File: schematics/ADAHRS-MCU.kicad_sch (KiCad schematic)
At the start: 1 part

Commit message: finished the symbol of MCU v1_01
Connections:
- net +1.5V: now reaches U-TMS570LS20216-EP1.1 (VCCIO)
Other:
- title: Ts570s -> TMS570LS MCU
- moved on the sheet: U-TMS570LS20216-EP1

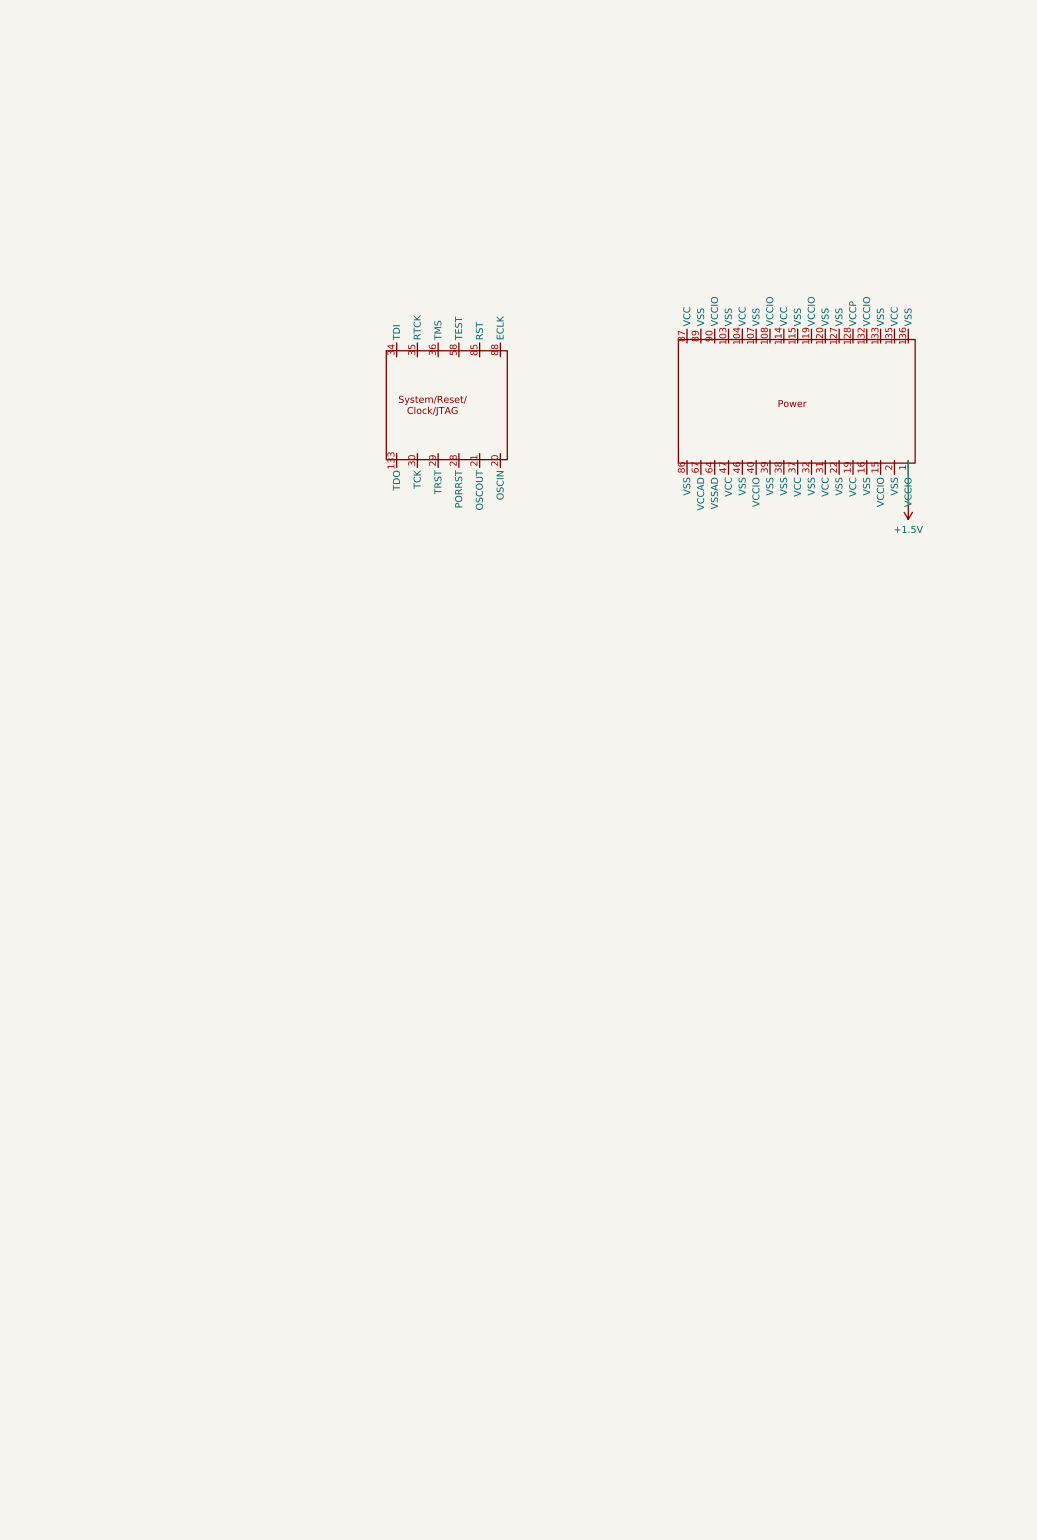
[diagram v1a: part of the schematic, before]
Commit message: finished wiring power and working on system v1.02
I had trouble with choosing and following the datasheet for the IC that supervises the supply. I had the option to doing hardware logic but it is suppose to be cheaper and having an IC suppose to be safer on the system instead of using logic.
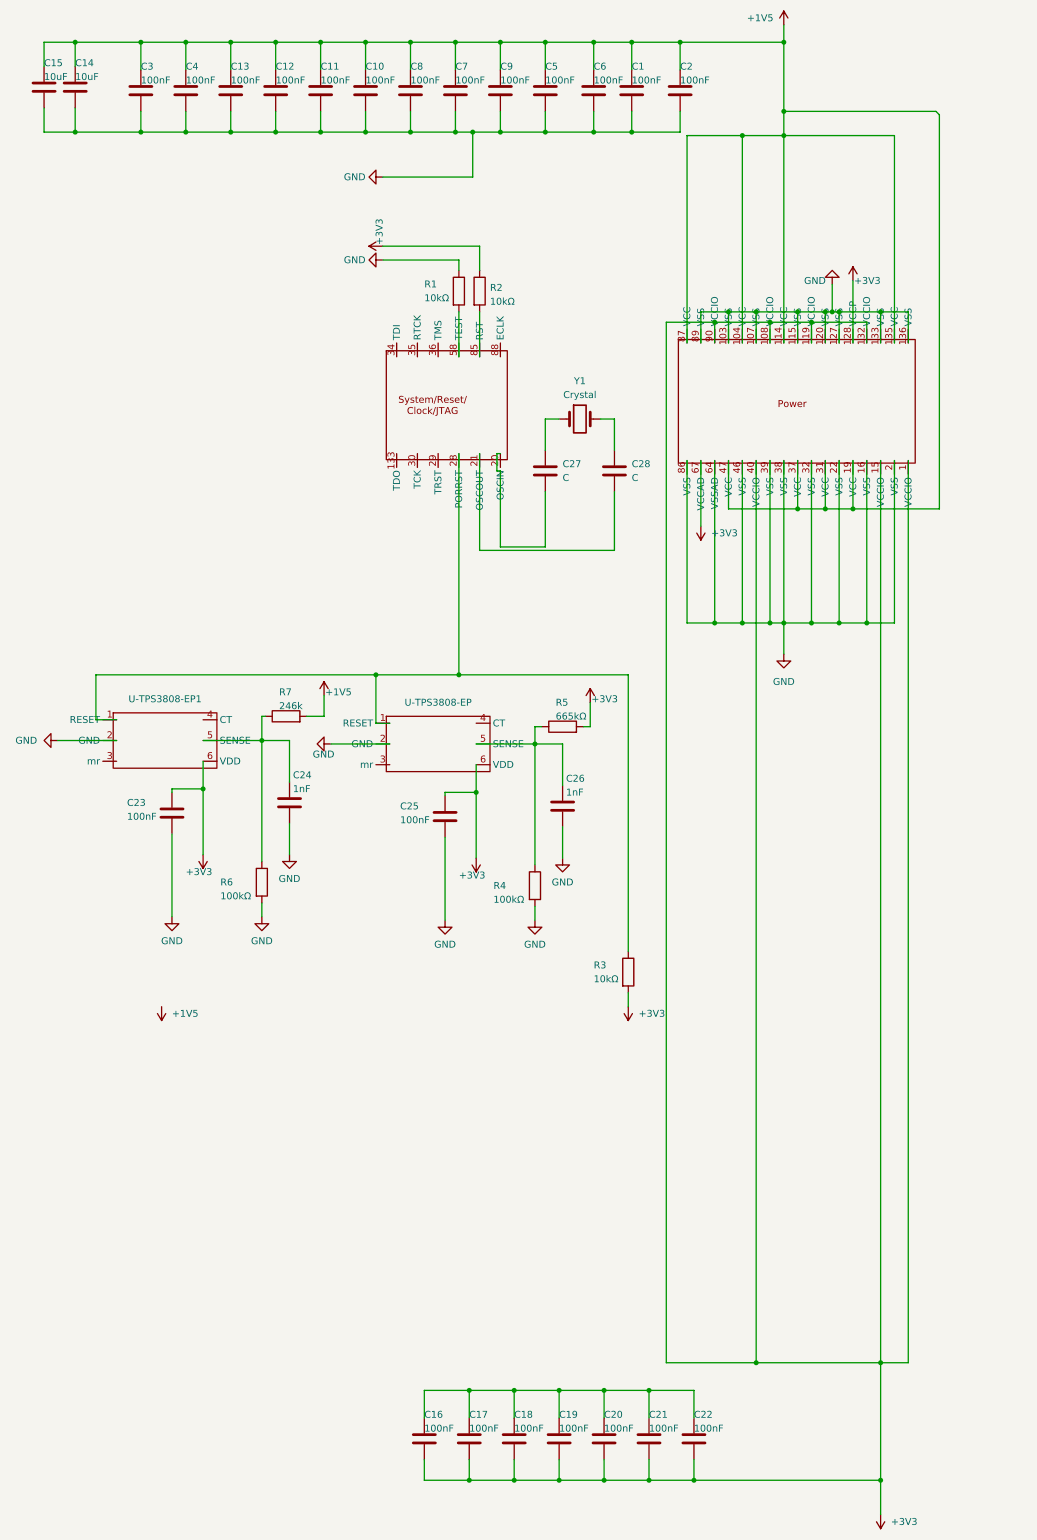
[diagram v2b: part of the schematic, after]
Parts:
- added C1, C10, C11, C12, C13, C16, C17, C18, C19, C2, C20, C21, C22, C23, C25, C3, C4, C5, C6, C7, C8, C9: 100nF, symbol Device:C
- added C14, C15: 10uF, symbol Device:C
- added C24, C26: 1nF, symbol Device:C
- added C27, C28: C, symbol Device:C
- added R1, R2, R3: 10kΩ, symbol Device:R
- added R4, R6: 100kΩ, symbol Device:R
- added R5: 665kΩ, symbol Device:R
- added R7: 246k, symbol Device:R
- added U-TPS3808-EP, U-TPS3808-EP1: ~, symbol custom:TPS3808-EP
- added Y1: Crystal, symbol Device:Crystal
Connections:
- net +1.5V is gone; now on net +3V3: U-TMS570LS20216-EP1.1 (VCCIO)
- net GND: now reaches U-TMS570LS20216-EP1.103 (VSS)
- net GND: now also U-TMS570LS20216-EP1.107 (VSS), U-TMS570LS20216-EP1.115 (VSS), U-TMS570LS20216-EP1.120 (VSS), U-TMS570LS20216-EP1.127 (VSS), U-TMS570LS20216-EP1.133 (VSS), U-TMS570LS20216-EP1.136 (VSS), U-TMS570LS20216-EP1.16 (VSS), U-TMS570LS20216-EP1.2 (VSS), U-TMS570LS20216-EP1.22 (VSS), U-TMS570LS20216-EP1.32 (VSS), U-TMS570LS20216-EP1.38 (VSS), U-TMS570LS20216-EP1.39 (VSS), U-TMS570LS20216-EP1.46 (VSS), U-TMS570LS20216-EP1.64 (VSSAD), U-TMS570LS20216-EP1.86 (VSS), U-TMS570LS20216-EP1.89 (VSS), C1.2, C10.2, C11.2, C12.2, C13.2, C14.2, C15.2, C2.2, C23.2, C24.2, C25.2, C26.2, C3.2, C4.2, C5.2, C6.2, C7.2, C8.2, C9.2, R1.1, R4.2, R6.2, U-TPS3808-EP.2 (GND), U-TPS3808-EP1.2 (GND)
- net +1V5: now reaches U-TMS570LS20216-EP1.104 (VCC)
- net +1V5: now also U-TMS570LS20216-EP1.114 (VCC), U-TMS570LS20216-EP1.135 (VCC), U-TMS570LS20216-EP1.19 (VCC), U-TMS570LS20216-EP1.31 (VCC), U-TMS570LS20216-EP1.37 (VCC), U-TMS570LS20216-EP1.47 (VCC), U-TMS570LS20216-EP1.87 (VCC), C1.1, C10.1, C11.1, C12.1, C13.1, C14.1, C15.1, C2.1, C3.1, C4.1, C5.1, C6.1, C7.1, C8.1, C9.1, R7.2
- net +3V3: now reaches U-TMS570LS20216-EP1.108 (VCCIO)
- net +3V3: now also U-TMS570LS20216-EP1.119 (VCCIO), U-TMS570LS20216-EP1.128 (VCCP), U-TMS570LS20216-EP1.132 (VCCIO), U-TMS570LS20216-EP1.15 (VCCIO), U-TMS570LS20216-EP1.40 (VCCIO), U-TMS570LS20216-EP1.67 (VCCAD), U-TMS570LS20216-EP1.90 (VCCIO), C16.2, C17.2, C18.2, C19.2, C20.2, C21.2, C22.2, C23.1, C25.1, R2.1, R3.2, R5.2, U-TPS3808-EP.6 (VDD), U-TPS3808-EP1.6 (VDD)
- net at U-TMS570LS20216-EP1.20 (OSCIN): now also C27.2
- net at U-TMS570LS20216-EP1.21 (OSCOUT): now also C28.2
- net at U-TMS570LS20216-EP1.28 (PORRST): now also R3.1, U-TPS3808-EP.1 (RESET), U-TPS3808-EP1.1 (RESET)
- net at U-TMS570LS20216-EP1.58 (TEST): now also R1.2
- net at U-TMS570LS20216-EP1.85 (RST): now also R2.2
- new net: C16.1, C17.1, C18.1, C19.1, C20.1, C21.1, C22.1
- new net: C26.1, R4.1, R5.1, U-TPS3808-EP.5 (SENSE)
- new net: C27.1, Y1.1
- new net: C28.1, Y1.2
- new net: C24.1, R6.1, R7.1, U-TPS3808-EP1.5 (SENSE)

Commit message: Finished JTAG connectors v1.03
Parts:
- added J1: Conn_02x05_Odd_Even, symbol Connector_Generic:Conn_02x05_Odd_Even
- C27, C28: value C -> 12pF
- R2: value 10kΩ -> 4.7kΩ
- Y1: value Crystal -> 16 MHz crystal osc
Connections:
- net GND: now also J1.3 (Pin_3), J1.5 (Pin_5), J1.9 (Pin_9)
- net at R2.2, U-TMS570LS20216-EP1.85 (RST): now also J1.10 (Pin_10)
- net at U-TMS570LS20216-EP1.30 (TCK): now also J1.4 (Pin_4)
- net at U-TMS570LS20216-EP1.34 (TDI): now also J1.8 (Pin_8)
- net at U-TMS570LS20216-EP1.36 (TMS): now also J1.2 (Pin_2)
- new net: J1.6 (Pin_6), U-TMS570LS20216-EP1.133 (VSS)
- new net +3.3V: J1.1 (Pin_1)
- no-connect marks 0 -> 7
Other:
- moved on the sheet: C1, C10, C11, C12, C13, C14, C15, C2, C27, C28, C3, C4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
